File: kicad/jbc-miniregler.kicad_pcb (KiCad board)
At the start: 2 copper layers, 110 x 100 mm, 180 parts, among them J1 Makita Plus, J10 Makita Minus, J12 ActivEnergy B2-, J13 ActivEnergy B1-, J2 Makita Minus, J4 USB_B, J5 AVR ISP, J6 ActivEnergy B2+, J7 ActivEnergy B1+, J8 Makita Plus, Q1 KND3508A, Q2 2N7002, Q3 MMBT3904, Q4 MMBT3904, Q5 ZXMP10A13FTA, SW1 UP, SW2 DOWN, SW3 ENTER, SW4 BACK, SW5 Reset, SW6 Ein/Aus, U1 OLED-128x32-Module, U10 MAX3232, U11 YD3082EESA, U12 TL431, U2 74LVC1G125, U3 NST175, U4 CH340C, U5 ATmega328P-AU, U6 GS8332-SR, U7 PN7006A, U8 XL7005A, U9 XL7005A, X1 POWER, X2 COM, X3 Lötkolben, X4 GND-Öse, Y1 16MHz

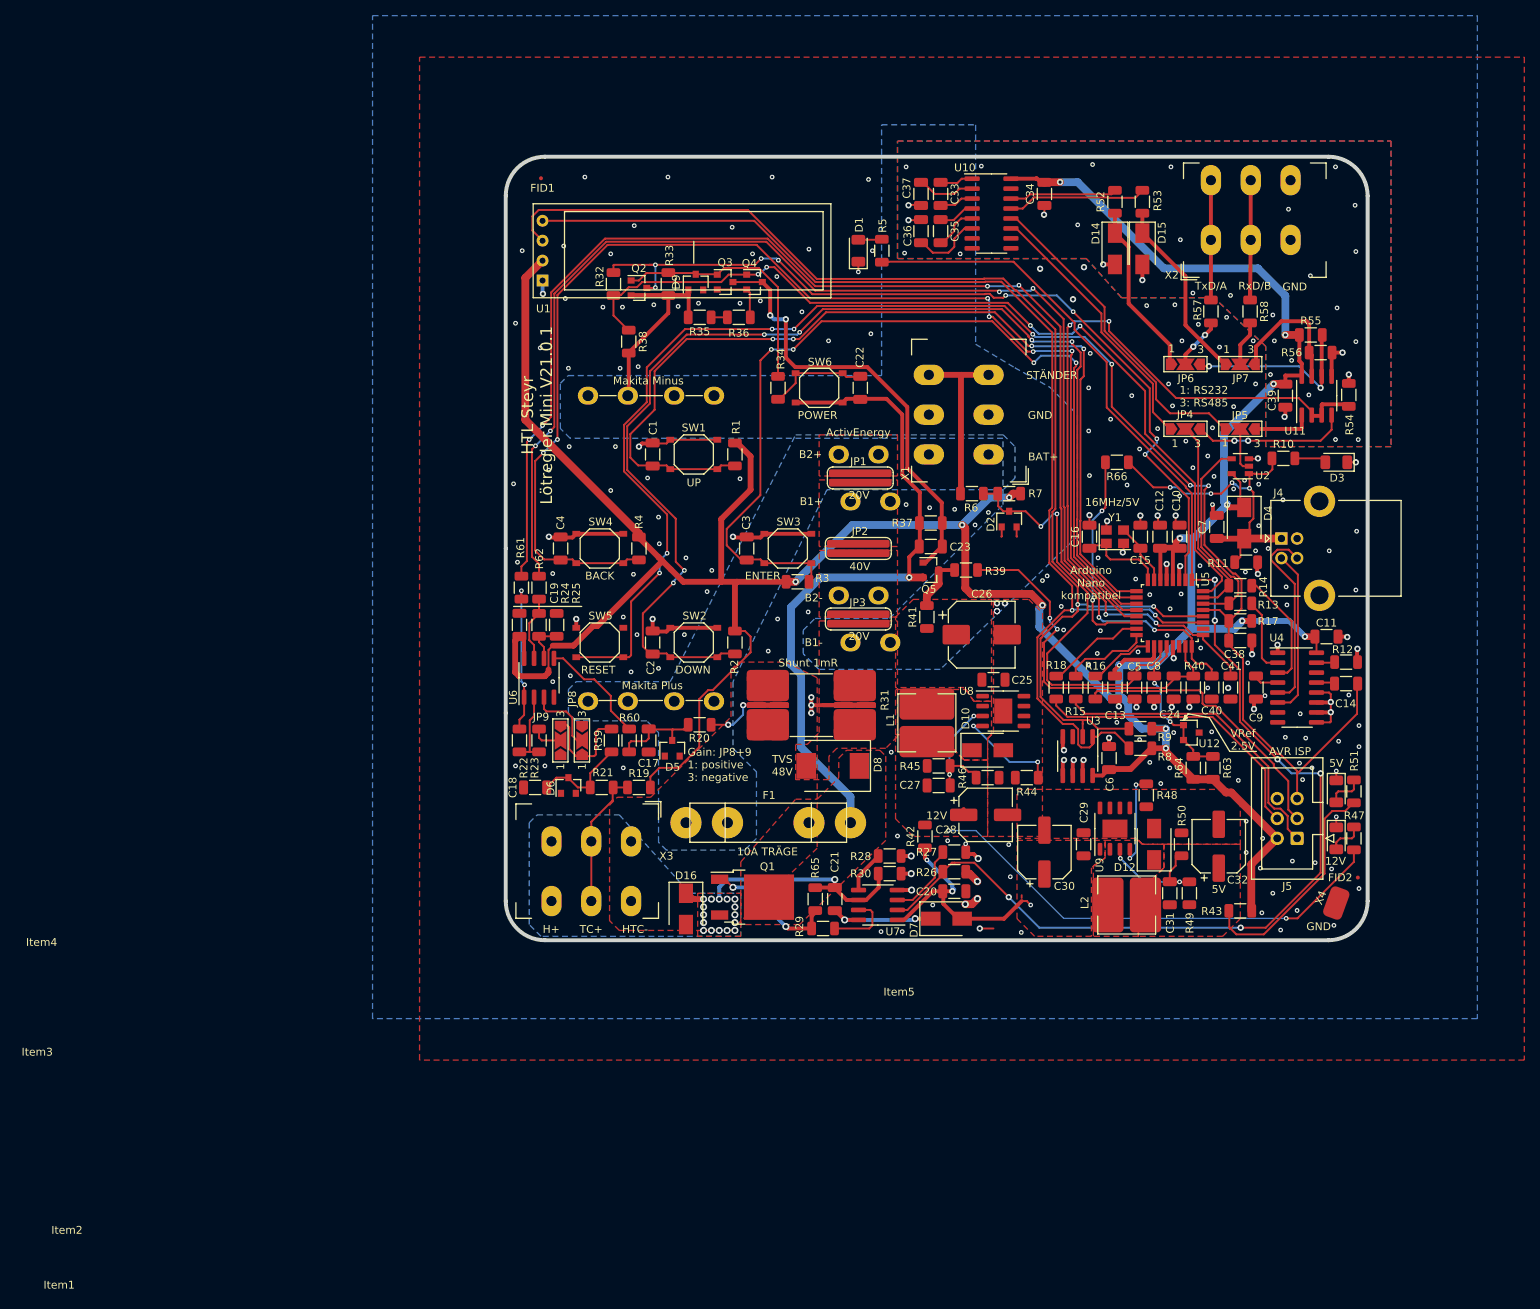
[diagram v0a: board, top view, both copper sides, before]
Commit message: umstellung auf pico als Main
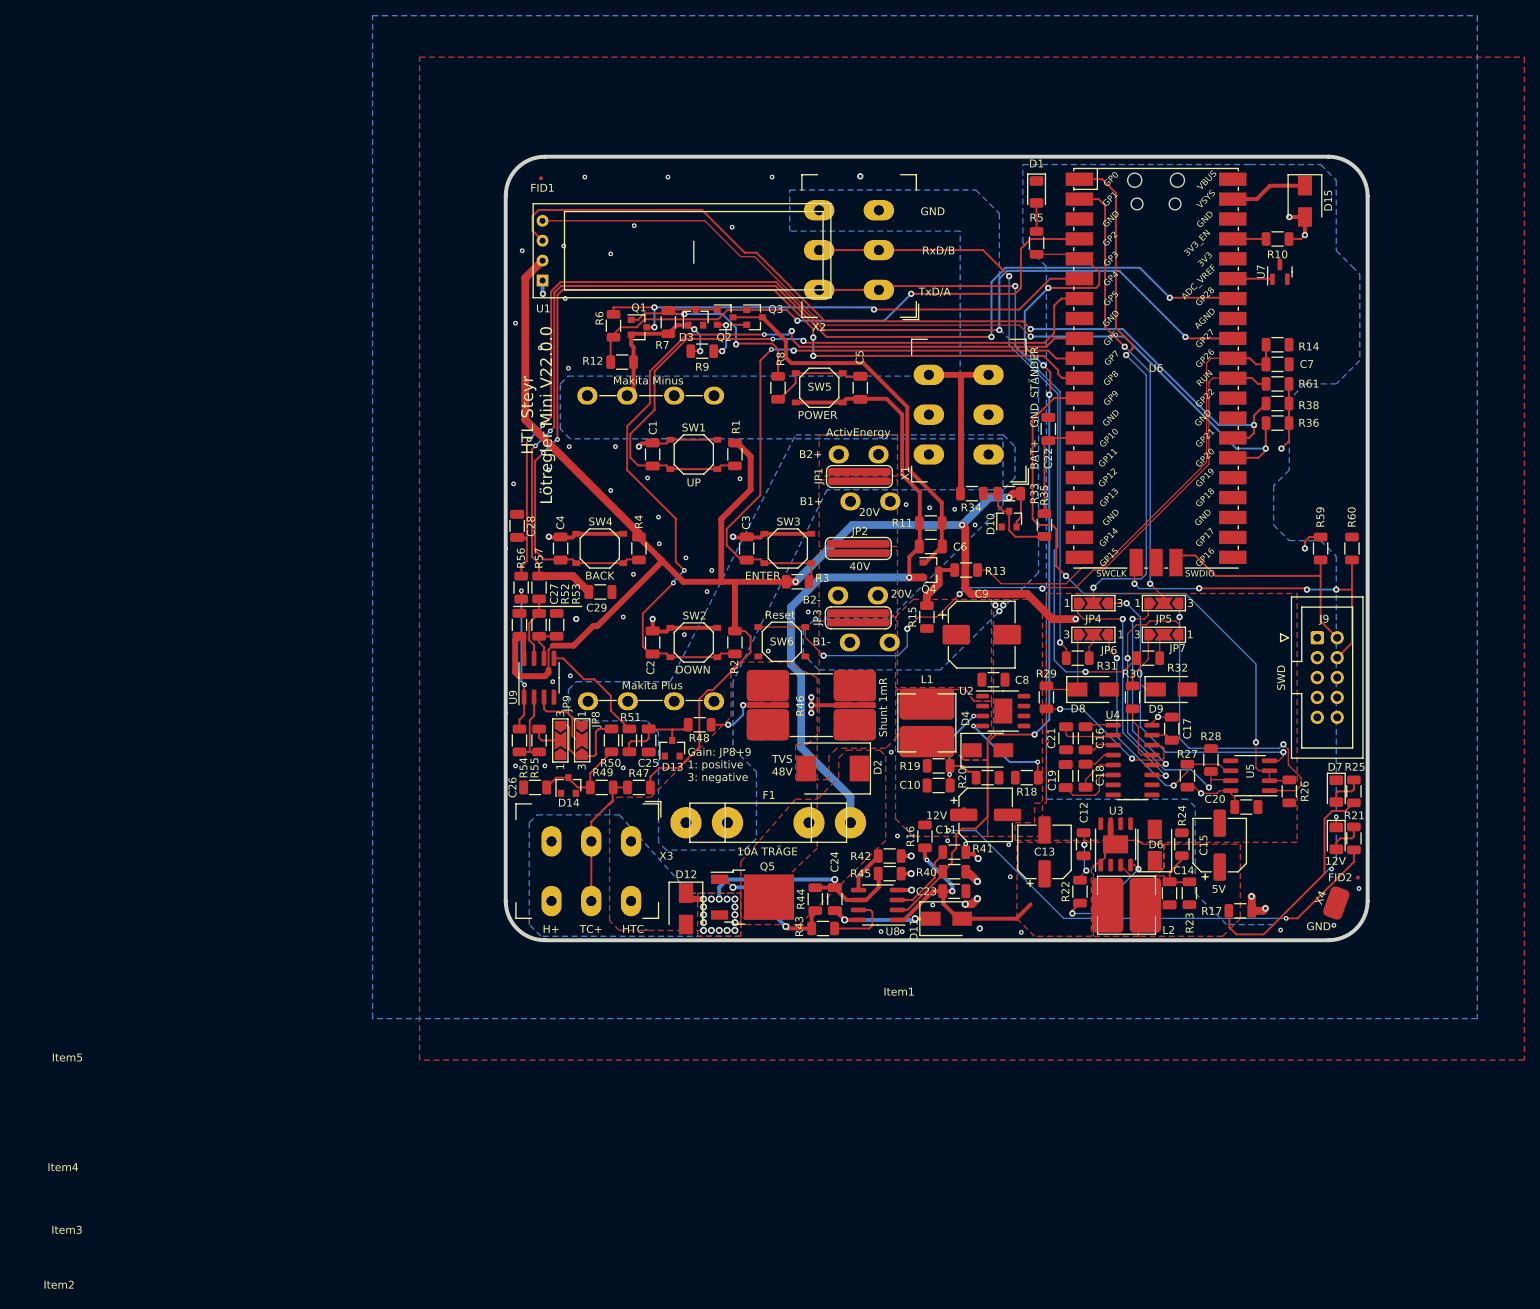
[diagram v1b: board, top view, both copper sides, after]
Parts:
- removed the C10 at (177.0, 91.5)
- removed the C11 at (195.8, 104.2)
- removed the C12 at (174.5, 91.5)
- removed C30, C32: 100u/25V, Capacitor_SMD:CP_Elec_6.3x5.9
- removed C31: 33n, Capacitor_SMD:C_1206_3216Metric
- removed C33, C34, C35, C36, C37, C39: 100n, Capacitor_SMD:C_1206_3216Metric
- removed C38, C40, C41: 10n, Capacitor_SMD:C_1206_3216Metric
- removed the C6 at (168.0, 119.8)
- removed the C7 at (181.8, 90.2)
- removed the C8 at (173.8, 110.8)
- removed the C9 at (186.8, 110.8)
- removed the D13 at (197.0, 124.0)
- removed D16: SS210, htl_smd:D_SMA_wide
- removed the D3 at (197.0, 82.0)
- removed the D4 at (185.2, 89.8)
- removed J10: Makita Minus, htl_connectors:Faston_Tab_6.3mm_vertical
- removed J12: ActivEnergy B2-, htl_connectors:Faston_Tab_6.3mm_vertical
- removed J13: ActivEnergy B1-, htl_connectors:Faston_Tab_6.3mm_vertical
- removed the J4 at (190.0, 91.7)
- removed the J5 at (192.0, 130.0)
- removed the R11 at (185.5, 94.8)
- removed the R12 at (198.2, 107.5)
- removed the R13 at (184.8, 100.0)
- removed the R14 at (184.8, 97.8)
- removed the R15 at (163.8, 110.8)
- removed the R16 at (166.2, 110.8)
- removed the R17 at (184.8, 102.2)
- removed the R18 at (161.2, 110.8)
- removed the R48 at (172.8, 124.5)
- removed R62: 100R, Resistor_SMD:R_1206_3216Metric
- removed R63, R64: 1k, Resistor_SMD:R_1206_3216Metric
- removed R65: 56k, Resistor_SMD:R_1206_3216Metric
- removed R66: 3k3, Resistor_SMD:R_1206_3216Metric
- removed the R8 at (172.0, 118.5)
- removed U10: MAX3232, Package_SO:SOIC-16_3.9x9.9mm_P1.27mm
- removed U11: YD3082EESA, Package_SO:SOIC-8_3.9x4.9mm_P1.27mm
- removed U12: TL431, Package_TO_SOT_SMD:SOT-23
- removed the U2 at (184.8, 82.5)
- removed the U3 at (164.0, 119.5)
- removed Y1: 16MHz, Crystal:Crystal_SMD_3225-4Pin_3.2x2.5mm
- added C17: 100n/50V, Capacitor_SMD:C_1206_3216Metric, F.Cu at (176.0, 116.0)
- added C18: 100n/50V, Capacitor_SMD:C_1206_3216Metric, F.Cu at (165.0, 122.0)
- added C19: 100n/50V, Capacitor_SMD:C_1206_3216Metric, F.Cu at (162.5, 122.0)
- added C20: 100n/50V, Capacitor_SMD:C_1206_3216Metric, F.Cu at (185.5, 126.0)
- added C21: 100n/50V, Capacitor_SMD:C_1206_3216Metric, F.Cu at (162.5, 117.2)
- added C28: 10n/50V, Capacitor_SMD:C_1206_3216Metric, F.Cu at (92.5, 90.1)
- added C29: 10n/50V, Capacitor_SMD:C_1206_3216Metric, F.Cu at (103.1, 98.6)
- added D6: SS210, htl_smd:D_SMA_wide, F.Cu at (173.8, 130.9)
- added D7: grün, LED_SMD:LED_1206_3216Metric, F.Cu at (197.0, 124.0)
- added D9: SMAJ8.0CA, Diode_SMD:D_SMA, F.Cu at (176.0, 111.0)
- added J6: Makita Minus, htl_connectors:Faston_Tab_6.3mm_vertical, B.Cu at (106.5, 73.5)
- added J7: ActivEnergy B2-, htl_connectors:Faston_Tab_6.3mm_vertical, B.Cu at (138.5, 99.0)
- added J8: ActivEnergy B1-, htl_connectors:Faston_Tab_6.3mm_vertical, B.Cu at (140.0, 105.0)
- added J9: SWD, Connector_IDC:IDC-Header_2x05_P2.54mm_Vertical, F.Cu at (194.6, 104.4)
- added R22: 100R, Resistor_SMD:R_1206_3216Metric, F.Cu at (164.3, 136.8)
- added R38: 3k3, Resistor_SMD:R_1206_3216Metric, F.Cu at (189.5, 74.5)
- added R44: 56k, Resistor_SMD:R_1206_3216Metric, F.Cu at (130.5, 137.8)
- added R50: 100R, Resistor_SMD:R_1206_3216Metric, F.Cu at (104.5, 117.5)
- added R51: 100R, Resistor_SMD:R_1206_3216Metric, F.Cu at (106.8, 117.5)
- added R56: 100R, Resistor_SMD:R_1206_3216Metric, F.Cu at (93.0, 98.0)
- added R57: 100R, Resistor_SMD:R_1206_3216Metric, F.Cu at (95.2, 98.0)
- added U6: Pico, RPi_Pico:RPi_Pico_SMD, F.Cu at (174.0, 70.0)
- added U7: LM4040CIM3-3.0/NOPB, Package_TO_SOT_SMD:SOT-23, F.Cu at (189.8, 57.7)
- C1, C2, C3, C4: value 100n -> 100n/50V
- C10: renamed from C27; value 33n -> 33n/50V
- C13: value 1u/100V -> 100u/25V; footprint Capacitor_SMD:C_1206_3216Metric -> Capacitor_SMD:CP_Elec_6.3x5.9
- C14: value 100n -> 33n/50V
- C15: value 12p -> 100u/25V; footprint Capacitor_SMD:C_1206_3216Metric -> Capacitor_SMD:CP_Elec_6.3x5.9
- C16: value 12p -> 100n/50V
- C22: renamed from C5; value 100n -> 100n/50V
- C25: renamed from C17; value 100n -> 100n/50V
- C26: renamed from C18; value 10n -> 10n/50V
- C27: renamed from C19; value 100n -> 100n/50V
- C6: renamed from C23; value 10n -> 10n/50V
- D15: value SMAJ8.0CA -> SS210; footprint Diode_SMD:D_SMA -> htl_smd:D_SMA_wide
- D3: renamed from D9; value 4V7 -> 3V3
- JP4, JP5: value UART -> COM
- R10: value 3k3 -> 100k
- R24: renamed from R50; value 3k3 -> 6k2
- R25: renamed from R51; value 3k3 -> 680R
- R33: renamed from R7; value 10k -> 82k
- R35: value 3k3 -> 100R
- R36: value 1k -> 3k3
- R59, R60: value 100R -> 100k
- R61: value 100R -> 10k
- R9: value 3k3 -> 2k7
- SW5: value Reset -> Ein/Aus
- SW6: value Ein/Aus -> RESET
- U4: value CH340C -> MAX3232
- U5: value ATmega328P-AU -> YD3082EESA; footprint Package_QFP:TQFP-32_7x7mm_P0.8mm -> Package_SO:SOIC-8_3.9x4.9mm_P1.27mm
- U8: renamed from U7; value PN7006A -> TF2101M-TAH
- moved R61 99.9 mm to (189.5, 72.0), turned to 180 degrees
- moved R60 95.4 mm to (199.0, 93.0), turned to -90 degrees
- moved R59 93.8 mm to (195.0, 93.0)
- moved R9 73.8 mm to (116.1, 67.8), turned to 0 degrees
- moved R36 70.1 mm to (189.5, 77.0), turned to 180 degrees
- moved R29 63.9 mm to (160.0, 112.0), turned to -90 degrees
- moved R30 63.3 mm to (171.0, 112.0), turned to -90 degrees
- moved D12 60.3 mm to (114.0, 139.0), turned to -90 degrees
- moved R27 58.4 mm to (178.0, 122.0), turned to 90 degrees
- moved D8 56.3 mm to (166.0, 111.0), turned to 0 degrees
- moved R28 53.9 mm to (181.0, 120.0), turned to 90 degrees
- moved X2 51.9 mm to (131.0, 60.0), turned to 90 degrees
- moved R35 51.4 mm to (159.8, 90.0), turned to 90 degrees
- moved R26 51.2 mm to (191.0, 124.0), turned to -90 degrees
- moved R31 47.4 mm to (164.0, 107.0), turned to 0 degrees
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- renumbered C28 to C11, C29 to C12, C20 to C23, C21 to C24, C22 to C5, C24 to C7, C25 to C8, C26 to C9, D2 to D10, D7 to D11, D5 to D13, D6 to D14, D8 to D2, D10 to D4, D11 to D5, D14 to D8, Item5 to Item1, Item1 to Item2, Item2 to Item3, Item3 to Item4, Item4 to Item5, J6 to J1, J7 to J2, J1 to J3, J8 to J4, J2 to J5, Q2 to Q1, Q3 to Q2, Q4 to Q3, Q5 to Q4, Q1 to Q5, R37 to R11, R38 to R12, R39 to R13, R40 to R14, R41 to R15, R42 to R16, R43 to R17, R44 to R18, R45 to R19, R46 to R20, R47 to R21, R49 to R23, R54 to R26, R55 to R27, R56 to R28, R52 to R29, R53 to R30, R57 to R31, R58 to R32, R6 to R34, R26 to R40, R27 to R41, R28 to R42, R29 to R43, R30 to R45, R31 to R46, R19 to R47, R20 to R48, R21 to R49, R24 to R52, R25 to R53, R22 to R54, R23 to R55, R32 to R6, R33 to R7, R34 to R8, U8 to U2, U9 to U3, U6 to U9
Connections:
- net /Messverstärker/Shunt renamed /Leistungsteil/U_Shunt
- net /Stromversorgung/BAT+ renamed /Batterie Varianten/Plus
- net /Stromversorgung/Spannungsregler 12V/~en renamed /Stromversorgung/Spannungsregler 12V/~{en}
- C13 pad 1: +5V -> /Leistungsteil/12V
- C13 pad 2: GND -> GNDPWR
- C14 pad 1: Net-(C14-Pad1) -> /Stromversorgung/Spannungsregler 3,3V/3,3V
- C14 pad 2: /Arduino/Arduino Nano/~RESET -> /Stromversorgung/Spannungsregler 3,3V/fb
- C15 pad 1: Net-(C15-Pad1) -> /Stromversorgung/Spannungsregler 3,3V/3,3V
- C15 pad 2: GND -> GNDPWR
- C16 pad 2: GND -> Net-(C16-Pad2)
- C22 pad 1: /Arduino/Arduino Nano/A6 -> Net-(C22-Pad1)
- C25 pad 2: Net-(C17-Pad2) -> Net-(C25-Pad2)
- C26 pad 1: Net-(C18-Pad1) (its old number) -> Net-(C26-Pad1)
- C27 pad 2: +5V -> +3.3V
- C5 pad 2: Net-(C22-Pad2) -> Net-(C5-Pad2)
- C7 pad 1: /Stromversorgung/BattMessung -> /Arduino/Batteriemessung
- D10 pad 2: GND -> +3.3V
- D10 pad 3: /Arduino/Arduino Nano/A6 -> Net-(D10-Pad3)
- D12 pad 1: /Stromversorgung/Spannungsregler 5V/sw -> /Leistungsteil/H+
- D12 pad 2: GNDPWR -> /Leistungsteil/HTC-
- D13 pad 3: Net-(C17-Pad2) -> Net-(C25-Pad2)
- D14 pad 3: Net-(C18-Pad1) (its old number) -> Net-(C26-Pad1)
- D15 pad 1: /UART RS232/RS485/RxD -> /Arduino/VSYS
- D15 pad 2: GNDPWR -> +3.3V
- JP6 pad 1: /UART RS232/RS485/TxD -> /UART RS232/RS485/A
- JP6 pad 3: /UART RS232/RS485/A -> /UART RS232/RS485/TxD
- JP7 pad 1: /UART RS232/RS485/RxD -> /UART RS232/RS485/B
- JP7 pad 3: /UART RS232/RS485/B -> /UART RS232/RS485/RxD
- JP8 pad 1: Net-(JP8-Pad1) -> GND
- JP8 pad 3: GND -> Net-(JP8-Pad3)
- JP9 pad 3: Net-(JP8-Pad1) -> Net-(JP8-Pad3)
- L2 pad 1: /Stromversorgung/Spannungsregler 5V/sw -> /Stromversorgung/Spannungsregler 3,3V/sw
- L2 pad 2: /Stromversorgung/Spannungsregler 5V/5V -> /Stromversorgung/Spannungsregler 3,3V/3,3V
- Q2 pad 2: Net-(Q3-Pad2) -> Net-(Q2-Pad2)
- Q3 pad 2: Net-(Q3-Pad2) -> Net-(Q2-Pad2)
- R1 pad 1: +5V -> +3.3V
- R10 pad 1: /Arduino/VUSB -> /Arduino/3V3_EN
- R10 pad 2: Net-(D3-Pad2) -> +3.3V
- R13 pad 2: /Stromversorgung/BattMessung -> /Arduino/Batteriemessung
- R14 pad 1: /Stromversorgung/BattMessung -> /Arduino/Batteriemessung
- R17 pad 1: +5V -> +3.3V
- R17 pad 2: /Stromversorgung/Spannungsregler 5V/5V -> /Stromversorgung/Spannungsregler 3,3V/3,3V
- R2 pad 1: +5V -> +3.3V
- R23 pad 1: /Stromversorgung/Spannungsregler 5V/5V -> /Stromversorgung/Spannungsregler 3,3V/3,3V
- R23 pad 2: /Stromversorgung/Spannungsregler 5V/fb -> /Stromversorgung/Spannungsregler 3,3V/fb
- R24 pad 1: /Stromversorgung/Spannungsregler 5V/fb -> /Stromversorgung/Spannungsregler 3,3V/fb
- R25 pad 1: /Stromversorgung/Spannungsregler 5V/5V -> /Stromversorgung/Spannungsregler 3,3V/3,3V
- R27 pad 1: +5V -> +3.3V
- R3 pad 1: +5V -> +3.3V
- R33 pad 1: +5V -> +3.3V
- R33 pad 2: /Arduino/Arduino Nano/A6 -> Net-(D10-Pad3)
- R34 pad 2: /Arduino/Arduino Nano/A6 -> Net-(D10-Pad3)
- R35 pad 1: Net-(R35-Pad1) -> Net-(D10-Pad3)
- R35 pad 2: GNDPWR -> Net-(C22-Pad1)
- R36 pad 1: Net-(R35-Pad1) -> +3.3V
- R36 pad 2: Net-(Q3-Pad2) -> /Arduino/SDA
- R4 pad 1: +5V -> +3.3V
- R47 pad 1: +5V -> +3.3V
- R48 pad 2: Net-(C17-Pad2) -> Net-(C25-Pad2)
- R49 pad 1: Net-(C18-Pad1) (its old number) -> Net-(C26-Pad1)
- R54 pad 1: Net-(R22-Pad1) -> Net-(R54-Pad1)
- R59 pad 1: Net-(C18-Pad1) (its old number) -> /Arduino/SWDIO
- R59 pad 2: Net-(JP8-Pad1) -> +3.3V
- R60 pad 1: Net-(C17-Pad2) -> GND
- R60 pad 2: Net-(R60-Pad2) -> /Arduino/SWCLK
- R61 pad 1: Net-(R22-Pad1) -> +3.3V
- R61 pad 2: /Arduino/Temperatur -> /Arduino/RUN
- R8 pad 1: Net-(C22-Pad2) -> Net-(C5-Pad2)
- R9 pad 1: +5V -> GNDPWR
- R9 pad 2: /Arduino/SCL -> Net-(Q2-Pad2)
- SW5 pad 1: GND -> Net-(C5-Pad2)
- SW5 pad 2: /Arduino/Arduino Nano/~RESET -> +BATT
- SW6 pad 1: Net-(C22-Pad2) -> /Arduino/RUN
- SW6 pad 2: +BATT -> GND
- U1 pad 2: +5V -> +3.3V
- U3 pad 2: /Stromversorgung/Spannungsregler 5V/sw -> /Stromversorgung/Spannungsregler 3,3V/sw
- U3 pad 3: /Stromversorgung/Spannungsregler 5V/fb -> /Stromversorgung/Spannungsregler 3,3V/fb
- U3 pad 4: /Stromversorgung/Spannungsregler 5V/~en -> /Stromversorgung/Spannungsregler 3,3V/~{en}
- U4 pad 1: GND -> Net-(C16-Pad1)
- U4 pad 10: GND -> unconnected-(U4-Pad10)
- U4 pad 11: GND -> /UART RS232/RS485/tin
- U4 pad 12: GND -> /UART RS232/RS485/rout
- U4 pad 13: Net-(C14-Pad1) -> /UART RS232/RS485/Rx
- U4 pad 14: (no net) -> /UART RS232/RS485/Tx
- U4 pad 15: Net-(R12-Pad1) -> GNDPWR
- U4 pad 16: +5V -> +3.3V
- U4 pad 3: Net-(R14-Pad2) -> Net-(C16-Pad2)
- U4 pad 5: /Arduino/Arduino Nano/D+ -> Net-(C18-Pad2)
- U4 pad 6: /Arduino/Arduino Nano/D- -> Net-(C19-Pad2)
- U4 pad 7: (no net) -> unconnected-(U4-Pad7)
- U4 pad 8: (no net) -> unconnected-(U4-Pad8)
- U4 pad 9: GND -> unconnected-(U4-Pad9)
- U5 pad 1: /Arduino/Heizelement -> /UART RS232/RS485/ro
- U5 pad 2: /Arduino/Ein-Aus-Taster -> /Arduino/ComDriverEnable
- U5 pad 3: GND -> /Arduino/ComDriverEnable
- U5 pad 4: +5V -> /UART RS232/RS485/di
- U5 pad 5: GND -> GNDPWR
- U5 pad 6: +5V -> /UART RS232/RS485/A
- U5 pad 7: Net-(C15-Pad1) -> /UART RS232/RS485/B
- U5 pad 8: Net-(C16-Pad1) -> +3.3V
- U9 pad 1: Net-(R22-Pad1) -> Net-(R54-Pad1)
- U9 pad 5: Net-(R60-Pad2) -> Net-(R51-Pad2)
- U9 pad 8: +5V -> +3.3V
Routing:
- net +5V: track 445.0 -> 0.00 mm, vias 14 -> 0
- net +3.3V: track 0.00 -> 250.5 mm, vias 0 -> 12
- net /Arduino/Arduino Nano/~RESET: track 202.6 -> 0.00 mm, vias 8 -> 0
- net /Arduino/RUN: track 0.00 -> 89.7 mm, vias 0 -> 4
- net /UART RS232/RS485/RxD_B: track 16.5 -> 89.3 mm, vias 0 -> 2
- net /Arduino/Heizelement: track 178.0 -> 112.0 mm, vias 6 -> 4
- net GND: track 124.2 -> 63.3 mm, vias 215 -> 71
- net /UART RS232/RS485/TxD_A: track 15.3 -> 75.4 mm, vias 0 -> 2
- net /Arduino/Batteriemessung: track 0.00 -> 59.7 mm
- net /Arduino/Arduino Nano/A6: track 55.8 -> 0.00 mm, vias 2 -> 0
- net /Arduino/SWCLK: track 0.00 -> 51.7 mm, vias 0 -> 4
- net /Arduino/RxD: track 6.16 -> 56.8 mm, vias 0 -> 2
- net /Stromversorgung/BattMessung: track 46.5 -> 0.00 mm, vias 2 -> 0
- net /Arduino/SCL: track 160.0 -> 116.0 mm
- net /Arduino/VUSB: track 44.0 -> 0.00 mm, vias 4 -> 0
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- added copper zone on B.Cu, net +3.3V
- added copper zone on F.Cu, net /Stromversorgung/Spannungsregler 3,3V/3,3V
- added copper zone on F.Cu, net /Stromversorgung/Spannungsregler 3,3V/sw
- removed copper zone on F.Cu, net /Stromversorgung/Spannungsregler 5V/5V
- removed copper zone on F.Cu, net /Stromversorgung/Spannungsregler 5V/sw
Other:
- net class 10A removed
- net class Default removed
- board text added: "HTL Steyr Lötregler Mini V22.0.0"
- board text added: "Reset"
- board text added: "SWD"
- board text removed: "16MHz/5V"
- board text removed: "1: RS232 3: RS485"
- board text removed: "AVR ISP"
- board text removed: "Arduino Nano kompatibel"
- board text removed: "HTL Steyr Lötregler Mini V21.0.1"
- board text removed: "MISO"
- board text removed: "MOSI"
- board text removed: "RESET"
- board text removed: "SCK"
- board text removed: "VRef 2.5V"
- board text removed: "~RESET"
